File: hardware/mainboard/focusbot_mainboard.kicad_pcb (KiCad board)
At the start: 2 copper layers, 64 x 70 mm, 52 parts, among them Q1 AO3401A, SW1 Power_Switch, U1 ESP32-S3-WROOM-1-N16R8, U2 TP4056, U3 DW01A, U4 FS8205A, U5 SY8089AAAC, U6 DRV8833PWP, U7 MAX98357A, U8 MPU-6050

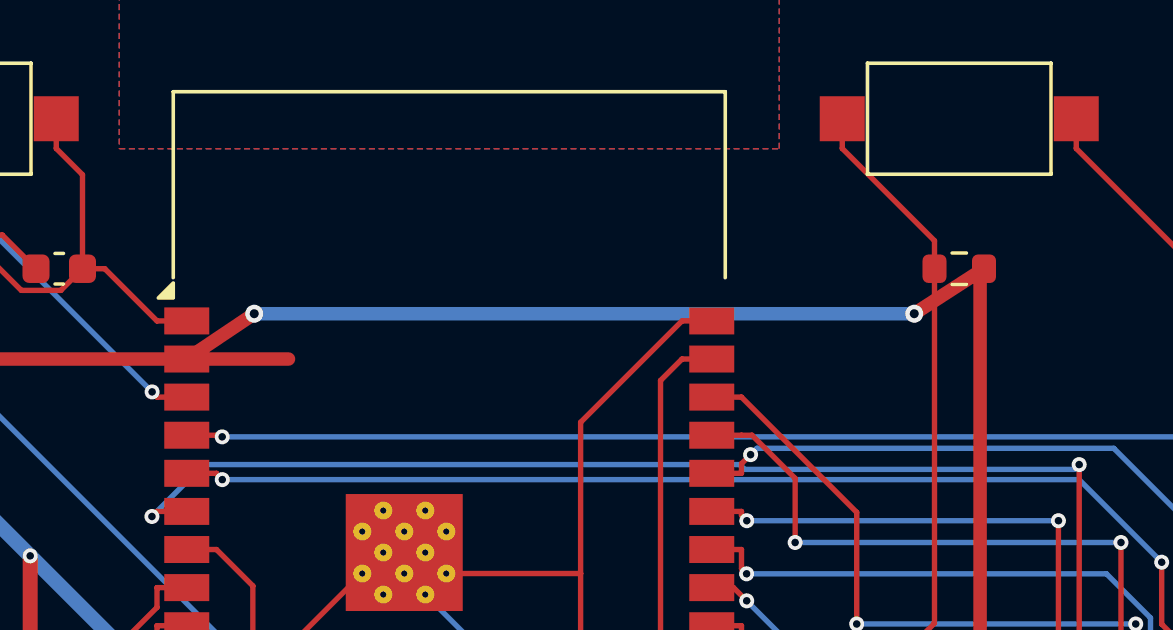
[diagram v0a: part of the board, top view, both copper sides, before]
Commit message: PCB: 0 DRC violations - fix 3V3 routing mainboard + clear headboard silkscreen overlaps
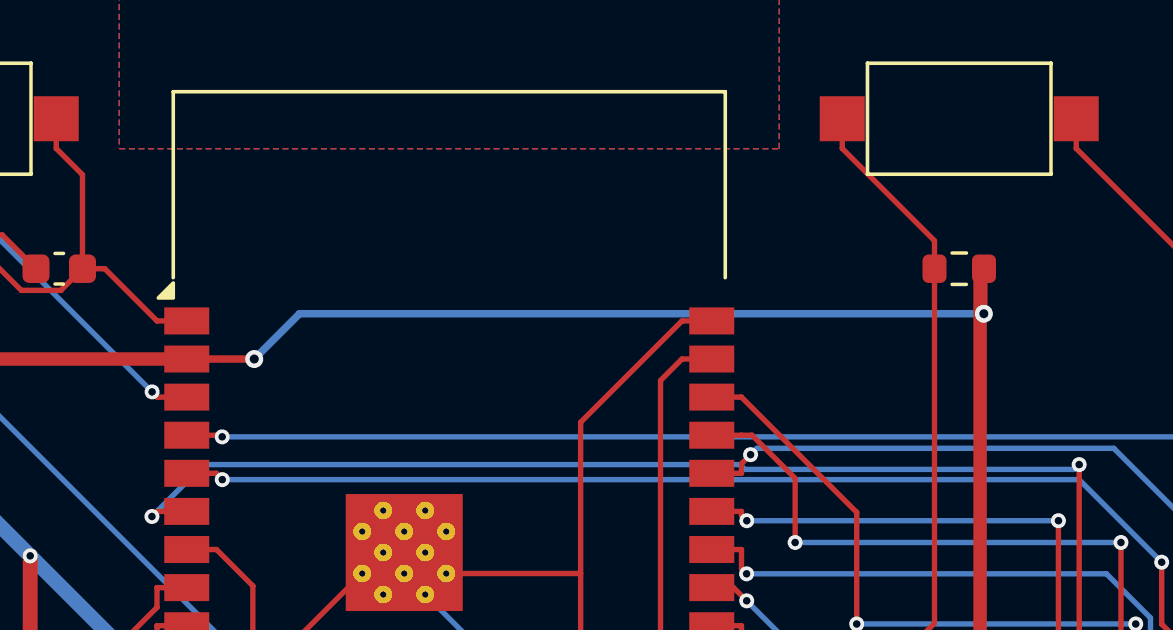
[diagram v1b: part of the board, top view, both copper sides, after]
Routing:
- net 3V3: track 170.0 -> 167.8 mm
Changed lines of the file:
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@@
-	)
-	(segment
-		(start 167.82 77)
-		(end 165.5 78.5)
-		(width 0.45)
-		(layer "F.Cu")
-		(net "3V3")
 	)
 	(segment
@@
 	)
 	(segment
-		(start 143.5 78.5)
-		(end 141.25 80.01)
-		(width 0.45)
-		(layer "F.Cu")
-		(net "3V3")
-	)
-	(segment
 		(start 172.1126 97.4638)
 		(end 167.6941 93.0453)
@@
 	)
 	(segment
+		(start 167.82 77)
+		(end 167.82 78.5)
+		(width 0.25)
+		(layer "F.Cu")
+		(net "3V3")
+	)
+	(segment
 		(start 167.6941 91.3713)
 		(end 167.6941 77.1309)
@@
 		(end 148.4637 107.8068)
 		(width 0.45)
+		(layer "F.Cu")
+		(net "3V3")
+	)
+	(segment
+		(start 143.5 80.01)
+		(end 141.25 80.01)
+		(width 0.25)
 		(layer "F.Cu")
 		(net "3V3")
@@
 	)
 	(segment
-		(start 144.6422 80.01)
-		(end 141.25 80.01)
-		(width 0.45)
-		(layer "F.Cu")
-		(net "3V3")
-	)
-	(segment
 		(start 165.3524 130.3726)
 		(end 163.787 130.3726)
@@
 	)
 	(via
-		(at 143.5 78.5)
+		(at 143.5 80.01)
 		(size 0.6)
 		(drill 0.3)
@@
 	)
 	(via
-		(at 165.5 78.5)
+		(at 167.82 78.5)
 		(size 0.6)
 		(drill 0.3)
@@
 	)
 	(segment
-		(start 165.5 78.5)
-		(end 143.5 78.5)
-		(width 0.45)
+		(start 145.01 78.5)
+		(end 143.5 80.01)
+		(width 0.25)
 		(layer "B.Cu")
 		(net "3V3")
+	)
+	(segment
+		(start 167.82 78.5)
+		(end 145.01 78.5)
+		(width 0.25)
+		(layer "B.Cu")
+		(net "3V3")
